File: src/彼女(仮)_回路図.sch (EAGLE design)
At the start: 55 parts, among them IC1 A3921, SW1 TVAF06-A020B-R, SW2 TVAF06-A020B-R, SW3 THAF01-NC-R, SW4 SS-12D00G3

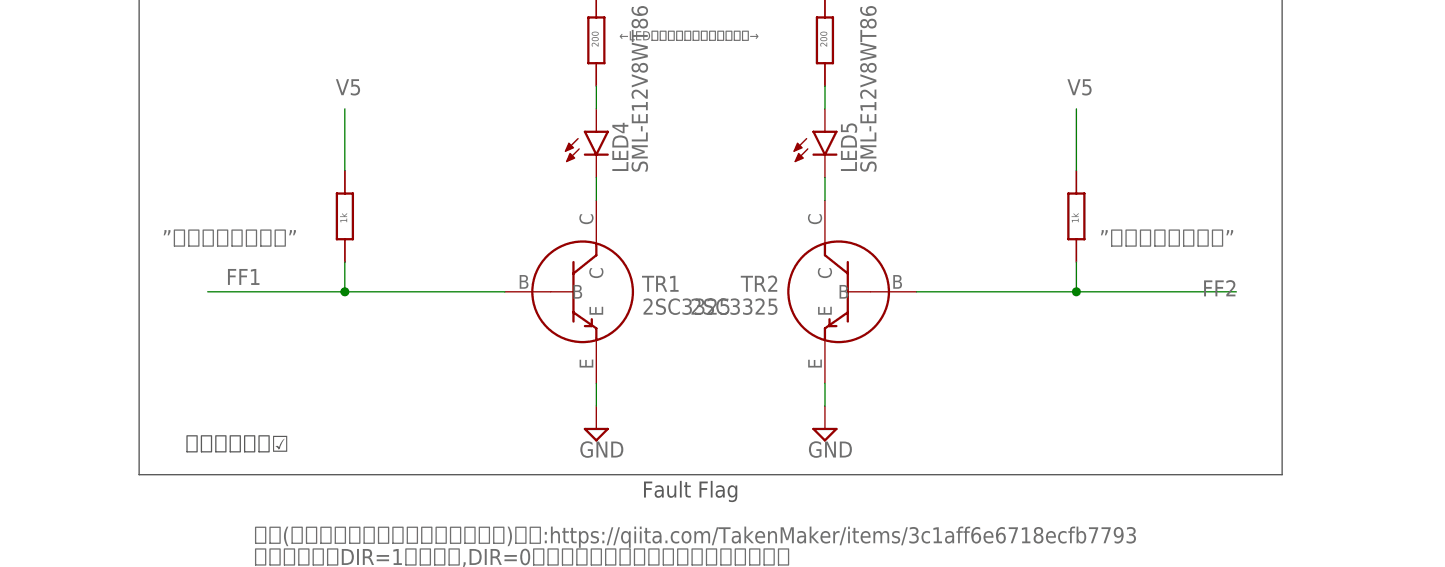
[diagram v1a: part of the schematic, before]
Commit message: edit:大体配線完了
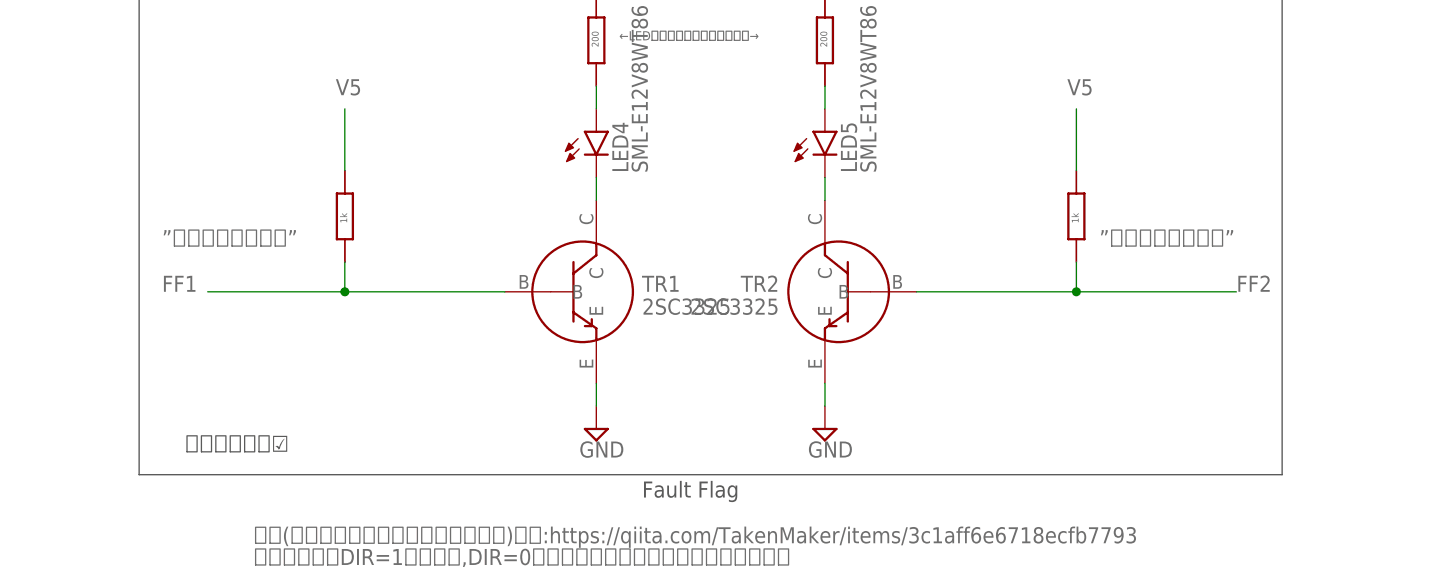
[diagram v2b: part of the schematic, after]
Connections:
- removed net N$19: R5.P$2, TR1.B
- removed net N$20: R6.P$2, TR2.B
- net FF1: now also R5.P$2, TR1.B
- net FF2: now also R6.P$2, TR2.B
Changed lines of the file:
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@@
 <text x="68.58" y="121.92" size="1.778" layer="95">パスコンくん</text>
 <text x="58.42" y="139.7" size="1.016" layer="95">プルアップ抵抗(RESETをGNDに接続するとRESET)</text>
-<text x="70.612" y="51.562" size="1.778" layer="95">FF1</text>
-<text x="179.07" y="50.292" size="1.778" layer="95">FF2</text>
 <text x="82.804" y="72.644" size="1.778" layer="95">V5</text>
 <text x="112.014" y="88.138" size="1.778" layer="95">V5</text>
@@
 <wire x1="101.6" y1="144.78" x2="96.52" y2="144.78" width="0.1524" layer="91"/>
 </segment>
+<segment>
+<wire x1="165.1" y1="50.8" x2="182.88" y2="50.8" width="0.1524" layer="91"/>
+<wire x1="165.1" y1="54.102" x2="165.1" y2="50.8" width="0.1524" layer="91"/>
+<wire x1="147.32" y1="50.8" x2="165.1" y2="50.8" width="0.1524" layer="91"/>
+<junction x="165.1" y="50.8"/>
+<pinref part="TR2" gate="G$1" pin="B"/>
+<pinref part="R6" gate="G$1" pin="P$2"/>
+<label x="182.88" y="50.8" size="1.778" layer="95"/>
+</segment>
 </net>
 <net name="FF1" class="0">
@@
 <pinref part="IC1" gate="G$1" pin="FF1"/>
 <wire x1="101.6" y1="142.24" x2="96.52" y2="142.24" width="0.1524" layer="91"/>
+</segment>
+<segment>
+<wire x1="68.58" y1="50.8" x2="83.82" y2="50.8" width="0.1524" layer="91"/>
+<pinref part="TR1" gate="G$1" pin="B"/>
+<wire x1="83.82" y1="50.8" x2="101.6" y2="50.8" width="0.1524" layer="91"/>
+<wire x1="83.82" y1="54.102" x2="83.82" y2="50.8" width="0.1524" layer="91"/>
+<junction x="83.82" y="50.8"/>
+<pinref part="R5" gate="G$1" pin="P$2"/>
+<label x="63.5" y="50.8" size="1.778" layer="95"/>
 </segment>
 </net>
@@
 </segment>
 </net>
-<net name="N$19" class="0">
-<segment>
-<wire x1="68.58" y1="50.8" x2="83.82" y2="50.8" width="0.1524" layer="91"/>
-<pinref part="TR1" gate="G$1" pin="B"/>
-<wire x1="83.82" y1="50.8" x2="101.6" y2="50.8" width="0.1524" layer="91"/>
-<wire x1="83.82" y1="54.102" x2="83.82" y2="50.8" width="0.1524" layer="91"/>
-<junction x="83.82" y="50.8"/>
-<pinref part="R5" gate="G$1" pin="P$2"/>
-</segment>
-</net>
-<net name="N$20" class="0">
-<segment>
-<wire x1="165.1" y1="50.8" x2="182.88" y2="50.8" width="0.1524" layer="91"/>
-<wire x1="165.1" y1="54.102" x2="165.1" y2="50.8" width="0.1524" layer="91"/>
-<wire x1="147.32" y1="50.8" x2="165.1" y2="50.8" width="0.1524" layer="91"/>
-<junction x="165.1" y="50.8"/>
-<pinref part="TR2" gate="G$1" pin="B"/>
-<pinref part="R6" gate="G$1" pin="P$2"/>
-</segment>
-</net>

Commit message: ビア,パターンの追加 ほぼ完成
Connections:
- net GND: now also EDGE1.P34, EDGE1.P35, EDGE1.P36, EDGE1.P37, EDGE1.P38, EDGE1.P39; no longer EDGE1.P18, EDGE1.P19, EDGE1.P20, EDGE1.P21, EDGE1.P22, EDGE1.P23
- net VCC: now also EDGE1.P18, EDGE1.P19, EDGE1.P20, EDGE1.P21, EDGE1.P22, EDGE1.P23; no longer EDGE1.P34, EDGE1.P35, EDGE1.P36, EDGE1.P37, EDGE1.P38, EDGE1.P39
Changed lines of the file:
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@@
 <attribute name="VALUE" x="15.875" y="123.825" size="1.778" layer="96"/>
 </instance>
-<instance part="P+4" gate="VCC" x="38.1" y="223.52" smashed="yes">
-<attribute name="VALUE" x="40.64" y="220.98" size="1.778" layer="96" rot="R90"/>
-</instance>
-<instance part="SUPPLY14" gate="GND" x="38.1" y="200.66" smashed="yes">
-<attribute name="VALUE" x="36.195" y="197.485" size="1.778" layer="96"/>
+<instance part="P+4" gate="VCC" x="12.7" y="218.44" smashed="yes">
+<attribute name="VALUE" x="15.24" y="215.9" size="1.778" layer="96" rot="R90"/>
+</instance>
+<instance part="SUPPLY14" gate="GND" x="38.1" y="198.12" smashed="yes">
+<attribute name="VALUE" x="36.195" y="194.945" size="1.778" layer="96"/>
 </instance>
 <instance part="SUPPLY15" gate="GND" x="289.56" y="124.46" smashed="yes">
@@
 </segment>
 <segment>
-<pinref part="P+4" gate="VCC" pin="VCC"/>
-<wire x1="38.1" y1="218.44" x2="38.1" y2="220.98" width="0.1524" layer="91"/>
+<pinref part="EDGE1" gate="G$1" pin="P18"/>
+<pinref part="EDGE1" gate="G$1" pin="P19"/>
+<wire x1="22.86" y1="200.66" x2="22.86" y2="203.2" width="0.1524" layer="91"/>
+<junction x="22.86" y="200.66"/>
+<wire x1="22.86" y1="198.12" x2="22.86" y2="200.66" width="0.1524" layer="91"/>
+<pinref part="EDGE1" gate="G$1" pin="P20"/>
+<junction x="22.86" y="198.12"/>
+<wire x1="22.86" y1="195.58" x2="22.86" y2="198.12" width="0.1524" layer="91"/>
+<pinref part="EDGE1" gate="G$1" pin="P21"/>
+<junction x="22.86" y="195.58"/>
+<wire x1="22.86" y1="193.04" x2="22.86" y2="195.58" width="0.1524" layer="91"/>
+<pinref part="EDGE1" gate="G$1" pin="P22"/>
+<junction x="22.86" y="193.04"/>
+<pinref part="EDGE1" gate="G$1" pin="P23"/>
+<wire x1="22.86" y1="190.5" x2="22.86" y2="193.04" width="0.1524" layer="91"/>
 <pinref part="EDGE1" gate="G$1" pin="P12"/>
-<pinref part="EDGE1" gate="G$1" pin="P17"/>
-<wire x1="22.86" y1="218.44" x2="22.86" y2="215.9" width="0.1524" layer="91"/>
+<wire x1="22.86" y1="203.2" x2="22.86" y2="205.74" width="0.1524" layer="91"/>
+<junction x="22.86" y="203.2"/>
 <pinref part="EDGE1" gate="G$1" pin="P13"/>
-<wire x1="22.86" y1="215.9" x2="22.86" y2="213.36" width="0.1524" layer="91"/>
+<wire x1="22.86" y1="205.74" x2="22.86" y2="208.28" width="0.1524" layer="91"/>
+<wire x1="22.86" y1="208.28" x2="22.86" y2="210.82" width="0.1524" layer="91"/>
+<wire x1="22.86" y1="210.82" x2="22.86" y2="213.36" width="0.1524" layer="91"/>
+<wire x1="22.86" y1="213.36" x2="22.86" y2="215.9" width="0.1524" layer="91"/>
+<wire x1="22.86" y1="215.9" x2="22.86" y2="218.44" width="0.1524" layer="91"/>
 <junction x="22.86" y="215.9"/>
 <pinref part="EDGE1" gate="G$1" pin="P14"/>
-<wire x1="22.86" y1="213.36" x2="22.86" y2="210.82" width="0.1524" layer="91"/>
 <junction x="22.86" y="213.36"/>
 <pinref part="EDGE1" gate="G$1" pin="P15"/>
-<wire x1="22.86" y1="210.82" x2="22.86" y2="208.28" width="0.1524" layer="91"/>
 <junction x="22.86" y="210.82"/>
 <pinref part="EDGE1" gate="G$1" pin="P16"/>
-<wire x1="22.86" y1="208.28" x2="22.86" y2="205.74" width="0.1524" layer="91"/>
 <junction x="22.86" y="208.28"/>
-<pinref part="EDGE1" gate="G$1" pin="P34"/>
-<wire x1="30.48" y1="205.74" x2="22.86" y2="205.74" width="0.1524" layer="91"/>
+<pinref part="EDGE1" gate="G$1" pin="P17"/>
 <junction x="22.86" y="205.74"/>
-<pinref part="EDGE1" gate="G$1" pin="P39"/>
-<wire x1="30.48" y1="218.44" x2="30.48" y2="215.9" width="0.1524" layer="91"/>
-<junction x="30.48" y="205.74"/>
-<pinref part="EDGE1" gate="G$1" pin="P38"/>
-<wire x1="30.48" y1="215.9" x2="30.48" y2="213.36" width="0.1524" layer="91"/>
-<junction x="30.48" y="215.9"/>
-<pinref part="EDGE1" gate="G$1" pin="P37"/>
-<wire x1="30.48" y1="213.36" x2="30.48" y2="210.82" width="0.1524" layer="91"/>
-<junction x="30.48" y="213.36"/>
-<pinref part="EDGE1" gate="G$1" pin="P36"/>
-<wire x1="30.48" y1="210.82" x2="30.48" y2="208.28" width="0.1524" layer="91"/>
-<junction x="30.48" y="210.82"/>
-<pinref part="EDGE1" gate="G$1" pin="P35"/>
-<wire x1="30.48" y1="208.28" x2="30.48" y2="205.74" width="0.1524" layer="91"/>
-<junction x="30.48" y="208.28"/>
-<wire x1="38.1" y1="218.44" x2="30.48" y2="218.44" width="0.1524" layer="91"/>
-<junction x="30.48" y="218.44"/>
+<pinref part="P+4" gate="VCC" pin="VCC"/>
+<wire x1="12.7" y1="215.9" x2="22.86" y2="215.9" width="0.1524" layer="91"/>
 </segment>
 </net>
@@
 </segment>
 <segment>
+<pinref part="EDGE1" gate="G$1" pin="P34"/>
+<pinref part="EDGE1" gate="G$1" pin="P39"/>
+<wire x1="30.48" y1="218.44" x2="30.48" y2="215.9" width="0.1524" layer="91"/>
+<pinref part="EDGE1" gate="G$1" pin="P38"/>
+<wire x1="30.48" y1="215.9" x2="30.48" y2="213.36" width="0.1524" layer="91"/>
+<junction x="30.48" y="215.9"/>
+<pinref part="EDGE1" gate="G$1" pin="P37"/>
+<wire x1="30.48" y1="213.36" x2="30.48" y2="210.82" width="0.1524" layer="91"/>
+<junction x="30.48" y="213.36"/>
+<pinref part="EDGE1" gate="G$1" pin="P36"/>
+<wire x1="30.48" y1="210.82" x2="30.48" y2="208.28" width="0.1524" layer="91"/>
+<junction x="30.48" y="210.82"/>
+<pinref part="EDGE1" gate="G$1" pin="P35"/>
+<wire x1="30.48" y1="208.28" x2="30.48" y2="205.74" width="0.1524" layer="91"/>
+<junction x="30.48" y="208.28"/>
 <pinref part="EDGE1" gate="G$1" pin="P28"/>
+<wire x1="30.48" y1="205.74" x2="30.48" y2="203.2" width="0.1524" layer="91"/>
+<junction x="30.48" y="205.74"/>
 <pinref part="EDGE1" gate="G$1" pin="P33"/>
-<wire x1="30.48" y1="190.5" x2="30.48" y2="193.04" width="0.1524" layer="91"/>
+<wire x1="30.48" y1="203.2" x2="30.48" y2="200.66" width="0.1524" layer="91"/>
+<junction x="30.48" y="203.2"/>
 <pinref part="EDGE1" gate="G$1" pin="P32"/>
-<wire x1="30.48" y1="193.04" x2="30.48" y2="195.58" width="0.1524" layer="91"/>
-<wire x1="30.48" y1="195.58" x2="30.48" y2="198.12" width="0.1524" layer="91"/>
-<wire x1="30.48" y1="198.12" x2="30.48" y2="200.66" width="0.1524" layer="91"/>
-<wire x1="30.48" y1="200.66" x2="30.48" y2="203.2" width="0.1524" layer="91"/>
+<wire x1="30.48" y1="200.66" x2="30.48" y2="198.12" width="0.1524" layer="91"/>
 <junction x="30.48" y="200.66"/>
 <pinref part="EDGE1" gate="G$1" pin="P31"/>
+<wire x1="30.48" y1="198.12" x2="30.48" y2="195.58" width="0.1524" layer="91"/>
 <junction x="30.48" y="198.12"/>
 <pinref part="EDGE1" gate="G$1" pin="P30"/>
+<wire x1="30.48" y1="195.58" x2="30.48" y2="193.04" width="0.1524" layer="91"/>
 <junction x="30.48" y="195.58"/>
 <pinref part="EDGE1" gate="G$1" pin="P29"/>
+<wire x1="30.48" y1="193.04" x2="30.48" y2="190.5" width="0.1524" layer="91"/>
 <junction x="30.48" y="193.04"/>
-<pinref part="EDGE1" gate="G$1" pin="P23"/>
-<wire x1="30.48" y1="190.5" x2="22.86" y2="190.5" width="0.1524" layer="91"/>
-<junction x="30.48" y="190.5"/>
-<pinref part="EDGE1" gate="G$1" pin="P18"/>
-<wire x1="22.86" y1="190.5" x2="22.86" y2="193.04" width="0.1524" layer="91"/>
-<junction x="22.86" y="190.5"/>
-<pinref part="EDGE1" gate="G$1" pin="P19"/>
-<wire x1="22.86" y1="193.04" x2="22.86" y2="195.58" width="0.1524" layer="91"/>
-<wire x1="22.86" y1="195.58" x2="22.86" y2="198.12" width="0.1524" layer="91"/>
-<wire x1="22.86" y1="198.12" x2="22.86" y2="200.66" width="0.1524" layer="91"/>
-<wire x1="22.86" y1="200.66" x2="22.86" y2="203.2" width="0.1524" layer="91"/>
-<junction x="22.86" y="200.66"/>
-<pinref part="EDGE1" gate="G$1" pin="P20"/>
-<junction x="22.86" y="198.12"/>
-<pinref part="EDGE1" gate="G$1" pin="P21"/>
-<junction x="22.86" y="195.58"/>
-<pinref part="EDGE1" gate="G$1" pin="P22"/>
-<junction x="22.86" y="193.04"/>
 <pinref part="SUPPLY14" gate="GND" pin="GND"/>
-<wire x1="30.48" y1="203.2" x2="38.1" y2="203.2" width="0.1524" layer="91"/>
-<junction x="30.48" y="203.2"/>
+<wire x1="38.1" y1="200.66" x2="30.48" y2="200.66" width="0.1524" layer="91"/>
 </segment>
 </net>
